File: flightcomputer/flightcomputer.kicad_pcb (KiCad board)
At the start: 4 copper layers, 100 x 75 mm, 63 parts, among them J1 Conn_Coaxial, J10 Conn_01x03, J11 Conn_01x03, J12 ESQ-113-14-G-D, J14 S3B-PH-K-S-GW, J2 Conn_Coaxial, J3 Conn_Coaxial, J4 Conn_Coaxial, J5 S3B-PH-K-S-GW, J6 Conn_01x03, J7 S4B-PH-K-S_LF__SN_, J8 Conn_01x03, J9 Conn_01x06, U1 MAX-M10S, U2 LIS2MDLTR, U3 BMI088, U4 MS5607-02BA, U7 Teensy4.1, U8 LSM6DSO32TR, U9 RFM96W-433S2

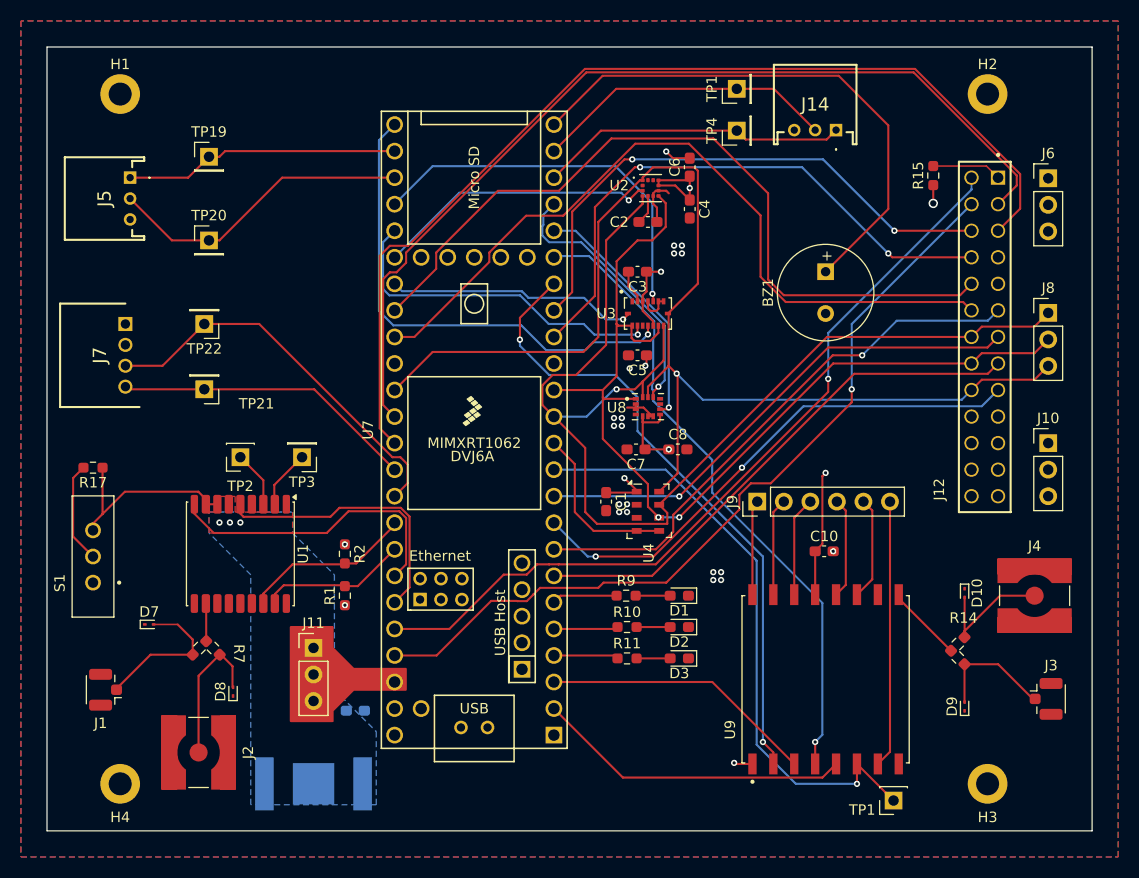
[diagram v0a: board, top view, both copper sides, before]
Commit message: changed coax diodes to 0603, reconfigure conn to add 3.3v, added indicator LEDs.
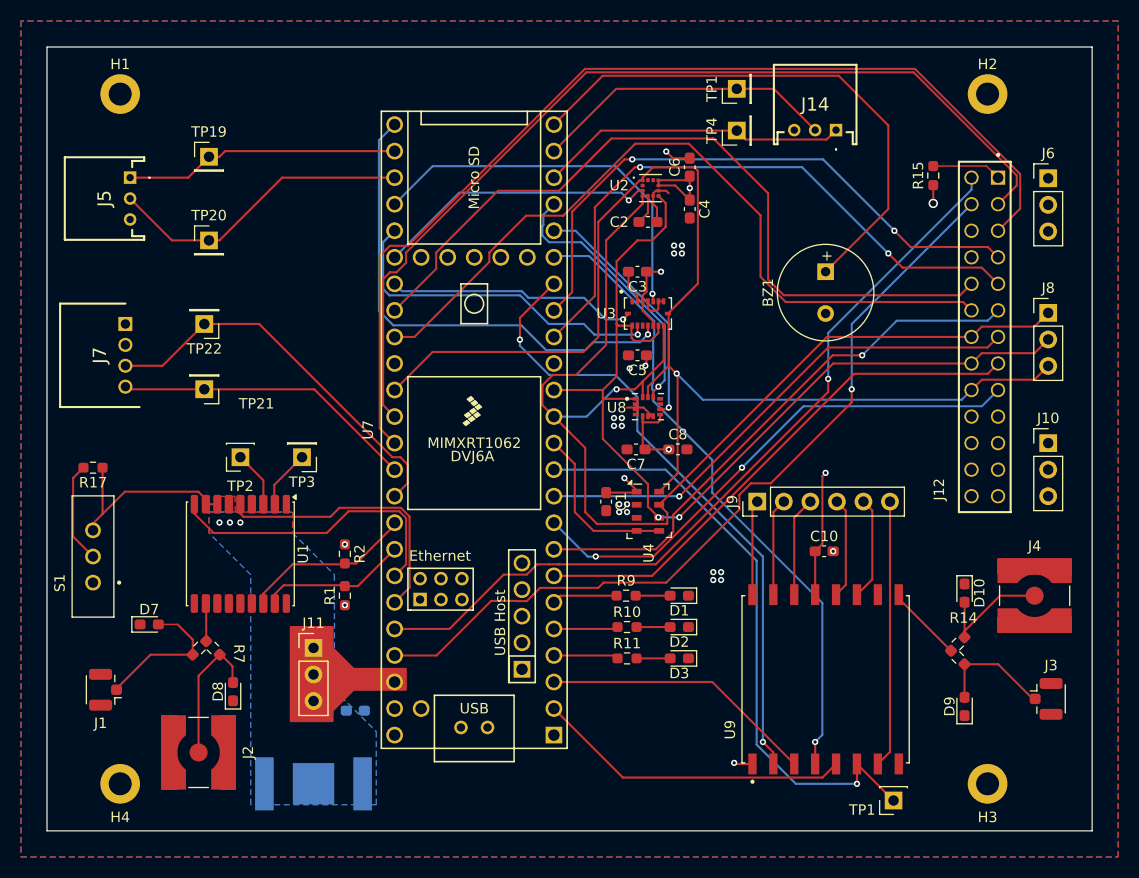
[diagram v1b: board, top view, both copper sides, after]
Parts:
- D10, D7, D8, D9: footprint Diode_SMD:D_SOD-923 -> Diode_SMD:D_0603_1608Metric_Pad1.05x0.95mm_HandSolder
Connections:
- J12 pad 06: /x_cursns -> /xV
- J12 pad 07: unconnected-(J12-Pad07) -> /x_cursns
- J12 pad 08: /x_fault -> /xV
- J12 pad 09: unconnected-(J12-Pad09) -> /x_fault
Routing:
- net /x_cursns: track 53.3 -> 56.9 mm
- net /x_fault: track 55.2 -> 58.8 mm

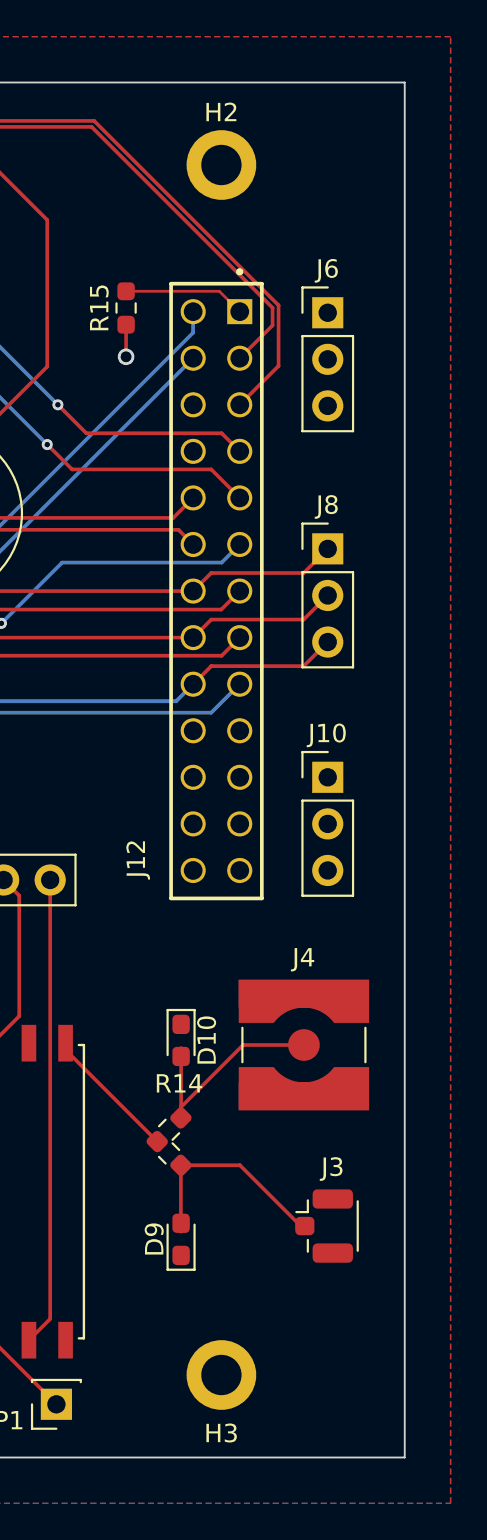
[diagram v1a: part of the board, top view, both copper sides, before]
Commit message: schematic notes and placement revisions for order
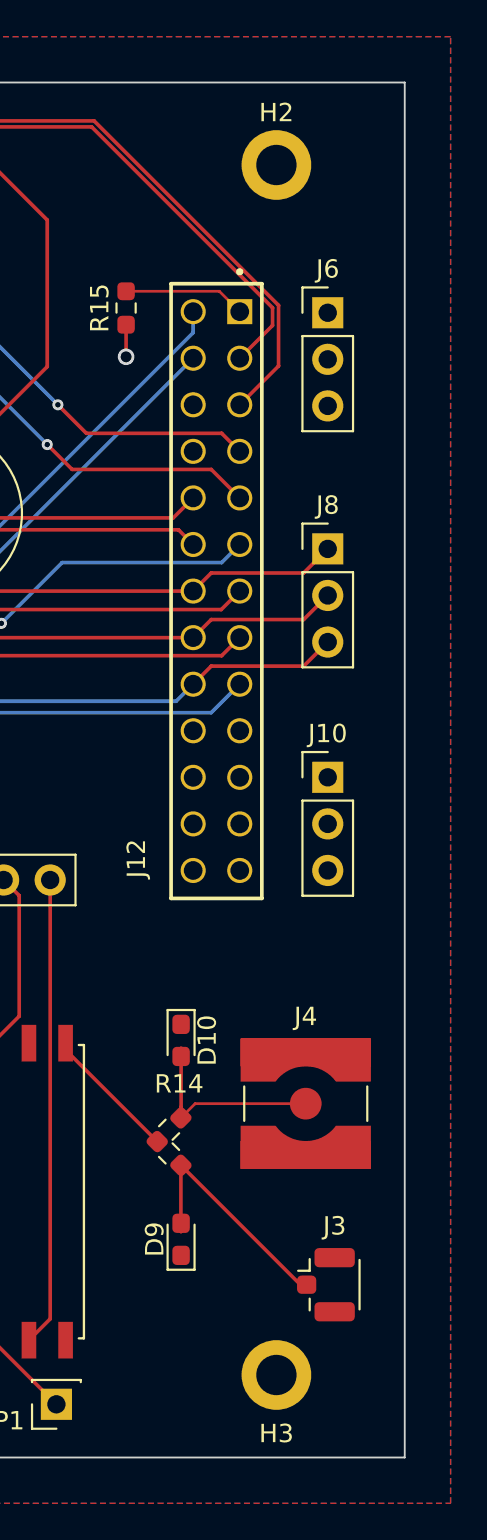
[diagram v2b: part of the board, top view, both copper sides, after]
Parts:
- moved J4 3.20 mm to (129.6, 118.2)
- moved J3 3.20 mm to (130.7, 128.1)
- moved H2 3.00 mm to (128.0, 67.0)
- moved H3 3.00 mm to (128.0, 133.0)
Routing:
- net Net-(D9-A2): track 11.7 -> 13.2 mm
- net Net-(D10-A2): track 12.5 -> 11.5 mm
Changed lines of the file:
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@@
 	(footprint "MountingHole:MountingHole_2.2mm_M2_DIN965_Pad"
 		(layer "F.Cu")
-		(at 125 133)
+		(at 128 133)
 		(descr "Mounting Hole 2.2mm, M2, generated by kicad-footprint-generator mountinghole.py")
 		(tags "mountinghole M2 DIN965")
@@
 	(footprint "Connector_Coaxial:U.FL_Hirose_U.FL-R-SMT-1_Vertical"
 		(layer "F.Cu")
-		(at 130.6 124.875)
+		(at 130.7 128.075)
 		(descr "Hirose U.FL Coaxial https://www.hirose.com/product/en/products/U.FL/U.FL-R-SMT-1%2810%29/")
 		(tags "Hirose U.FL Coaxial")
@@
 			(polygon
 				(pts
-					(xy 132.175 123.925) (xy 130.085 123.925) (xy 130.085 125.825) (xy 132.175 125.825)
+					(xy 132.275 127.125) (xy 130.185 127.125) (xy 130.185 129.025) (xy 132.275 129.025)
 				)
 			)
@@
 	(footprint "Connector_Coaxial:SMA_Amphenol_132134-10_Vertical"
 		(layer "F.Cu")
-		(at 129.5 115)
+		(at 129.6 118.2)
 		(descr "https://www.amphenolrf.com/library/download/link/link_id/596219/parent/132134-10/")
 		(tags "SMA SMD Female Jack Vertical")
@@
 	(footprint "MountingHole:MountingHole_2.2mm_M2_DIN965_Pad"
 		(layer "F.Cu")
-		(at 125 67)
+		(at 128 67)
 		(descr "Mounting Hole 2.2mm, M2, generated by kicad-footprint-generator mountinghole.py")
 		(tags "mountinghole M2 DIN965")
@@
 	)
 	(segment
-		(start 126.008672 121.558672)
-		(end 129.45 125)
+		(start 129.306798 128.075)
+		(end 129.65 128.075)
 		(width 0.2)
 		(layer "F.Cu")
@@
 	)
 	(segment
-		(start 122.79047 121.558672)
-		(end 126.008672 121.558672)
+		(start 122.79047 125.17047)
+		(end 122.8 125.18)
 		(width 0.2)
 		(layer "F.Cu")
@@
 	)
 	(segment
-		(start 122.79047 125.17047)
-		(end 122.8 125.18)
+		(start 122.79047 121.558672)
+		(end 129.306798 128.075)
 		(width 0.2)
 		(layer "F.Cu")
@@
 	)
 	(segment
-		(start 122.79047 118.392622)
-		(end 126.183092 115)
+		(start 122.8 118.968202)
+		(end 122.79047 118.977732)
 		(width 0.2)
 		(layer "F.Cu")
@@
 	)
 	(segment
-		(start 122.8 118.968202)
-		(end 122.79047 118.977732)
-		(width 0.2)
+		(start 129.6 118.2)
+		(end 123.568202 118.2)
+		(width 0.15)
 		(layer "F.Cu")
 		(net 15)
@@
 	)
 	(segment
-		(start 126.183092 115)
-		(end 129.5 115)
-		(width 0.2)
+		(start 123.568202 118.2)
+		(end 122.79047 118.977732)
+		(width 0.15)
 		(layer "F.Cu")
 		(net 15)

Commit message: fixes
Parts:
- added S2: EG1218, HPRlibrary:SW_EG1218, F.Cu at (109.3, 99.6)
- moved D9 4.83 mm to (127.4, 127.1)
- moved D10 3.26 mm to (124.8, 117.3)
- moved D7 3.15 mm to (44.0, 120.8), turned to -90 degrees
- moved D8 2.12 mm to (50.7, 124.6), turned to 180 degrees
- moved R15 0.40 mm to (119.8, 74.4)
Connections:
- C10 pad 1: /teensy_3.3v -> /radio_3.3v
- U9 pad 13: /teensy_3.3v -> /radio_3.3v
- U9 pad 2: /radio_mosi -> /radio_miso
- U9 pad 3: /radio_miso -> /radio_mosi
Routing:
- net /radio_3.3v: track 0.00 -> 16.7 mm, vias 0 -> 1
- net /teensy_3.3v: track 54.3 -> 42.6 mm, vias 9 -> 8
- net Net-(D7-A2): track 14.6 -> 8.78 mm
- net Net-(D10-A2): track 11.5 -> 7.73 mm
- net Net-(D9-A2): track 13.2 -> 9.56 mm
- net Net-(D8-A2): track 13.9 -> 10.3 mm
- net /xV: track 0.00 -> 2.54 mm
- net /x_cursns: track 56.9 -> 57.8 mm
- net /radio_mosi: track 61.0 -> 61.9 mm
- net /radio_miso: track 26.2 -> 25.4 mm
- net /PYRO2: track 50.9 -> 51.6 mm
- net Net-(J12-Pad01): track 6.66 -> 7.23 mm

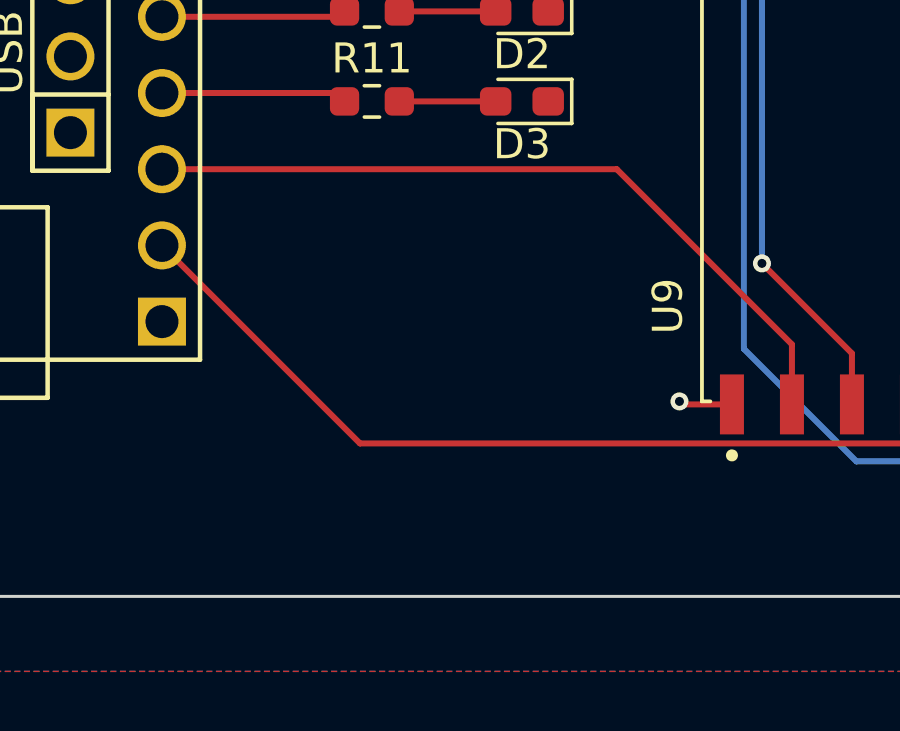
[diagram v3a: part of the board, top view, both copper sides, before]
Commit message: add jst 2pin for 5V fc
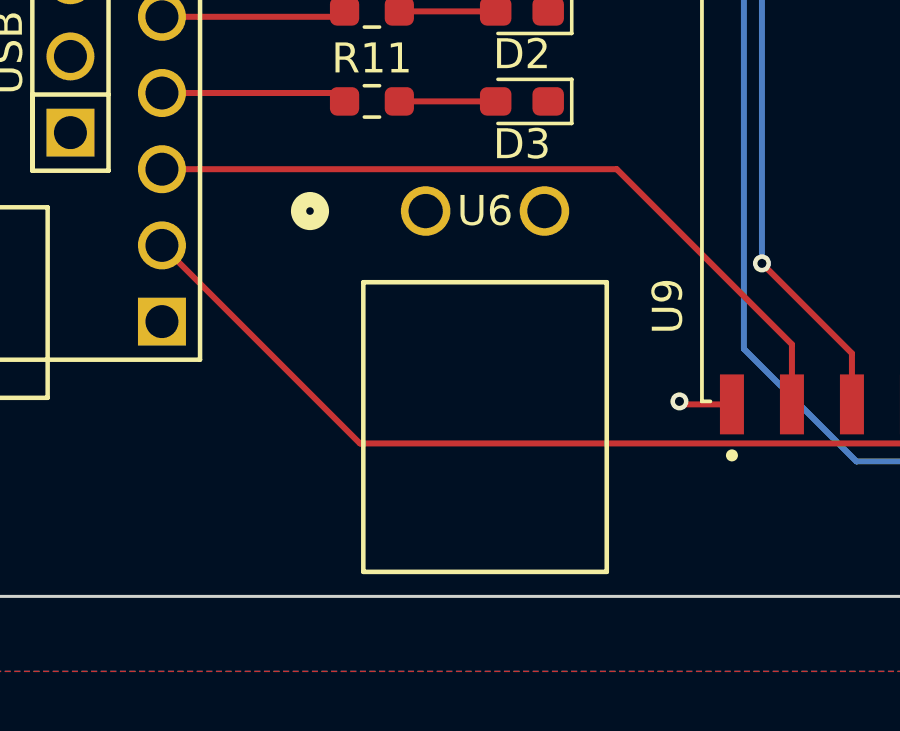
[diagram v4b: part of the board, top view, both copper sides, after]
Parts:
- added U6: S2P-VH, HPRlibrary:S2P-VH_JST, F.Cu at (92.3, 124.7)
